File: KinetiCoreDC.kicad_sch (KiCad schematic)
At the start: 7 parts, among them J1 TC2070-IDC-NL, SW1 PTS647, U1 STM32G070KBT6

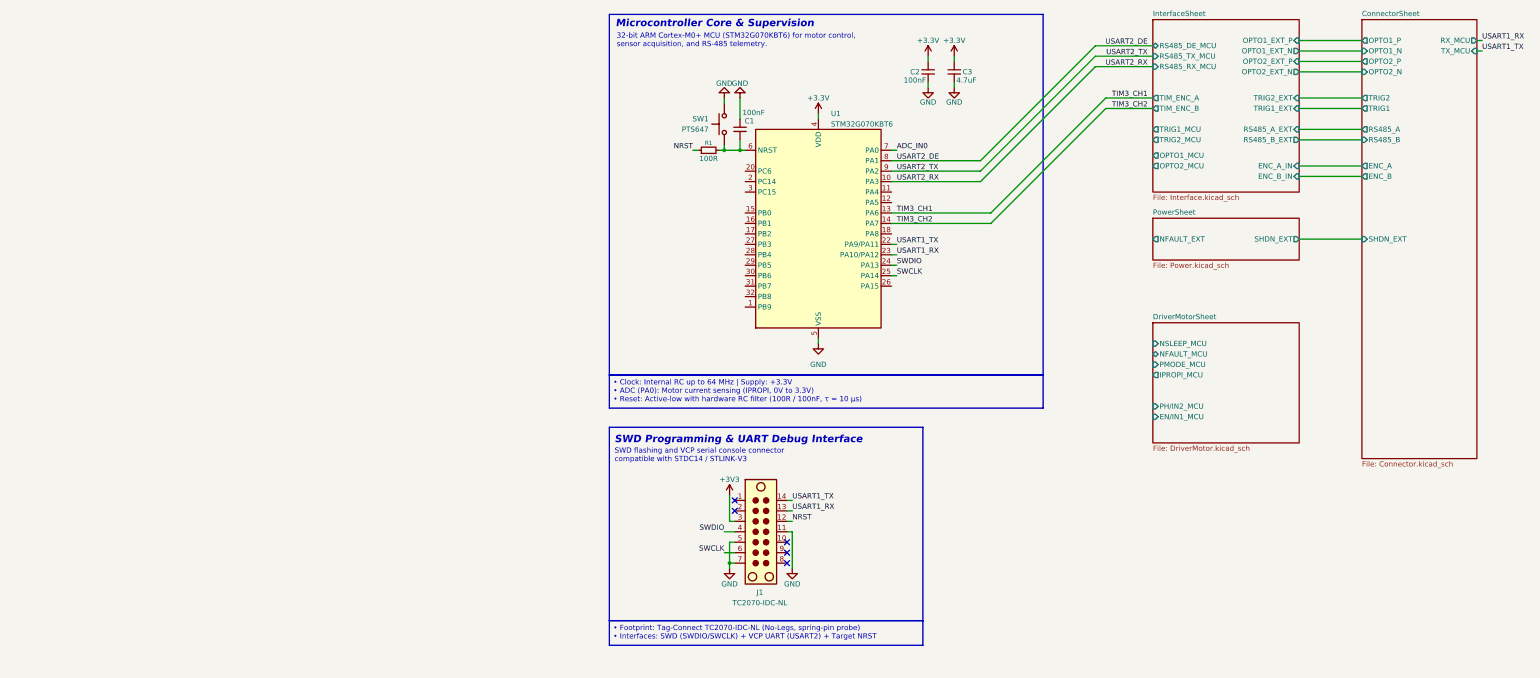
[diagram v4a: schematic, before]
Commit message: refactor(schematic): migrate MCU to LQFP48 and finalize pinout mapping
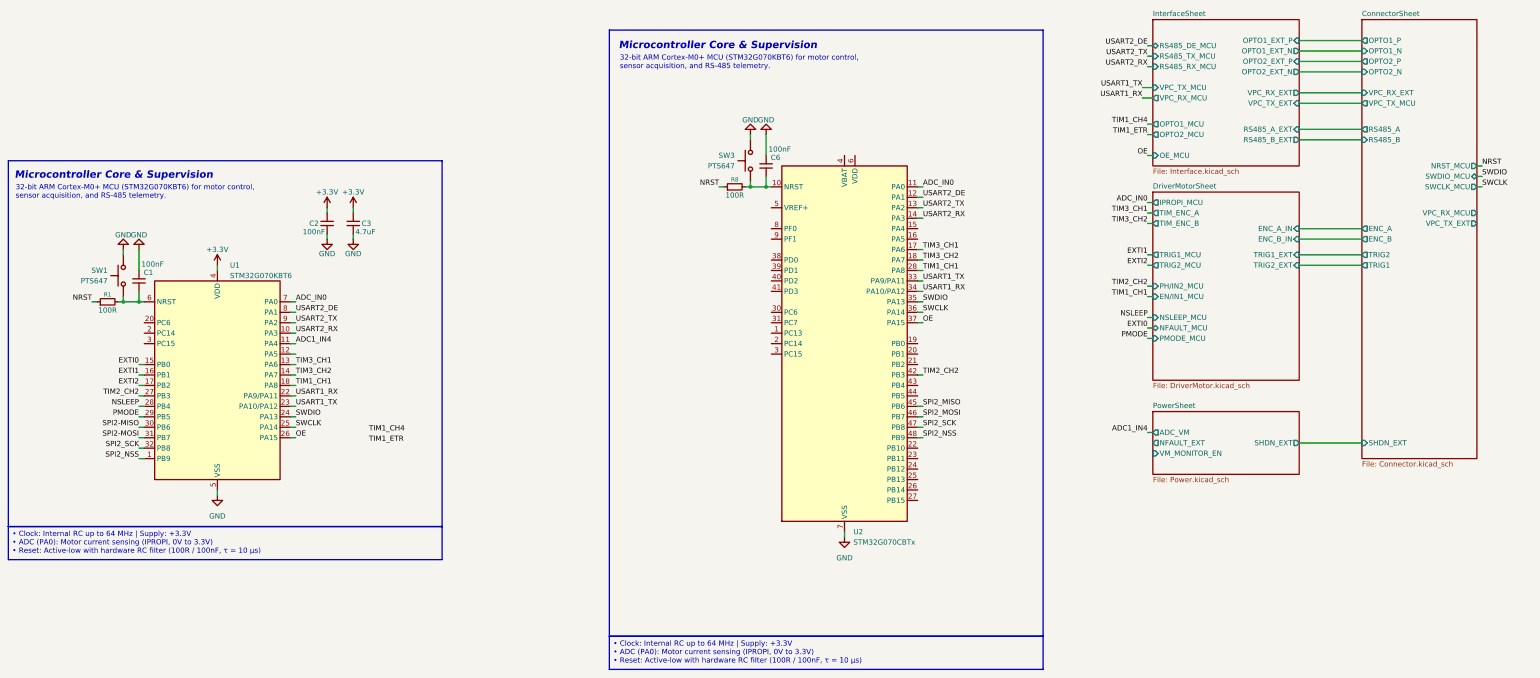
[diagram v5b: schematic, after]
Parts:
- removed J1: TC2070-IDC-NL, KineticCore:Tag-Connect_TC2070-IDC-FP_2x07_P1.27mm_Vertical, symbol Connector:TC2070
- added C6: 100nF, Capacitor_SMD:C_0603_1608Metric, symbol Device:C_Small
- added R8: 100R, Resistor_SMD:R_0603_1608Metric, symbol Device:R_Small
- added SW3: PTS647, Button_Switch_SMD:SW_SPST_PTS647_Sx38, symbol Switch:SW_Push
- added U2: STM32G070CBTx, Package_QFP:LQFP-48_7x7mm_P0.5mm, symbol MCU_ST_STM32G0:STM32G070CBTx
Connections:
- net ADC_IN0: now also U2.11 (PA0)
- net GND: now also C6.2, SW3.1, U2.7 (VSS)
- net NRST: now also R8.1
- net SWCLK: now also U2.36 (PA14)
- net SWDIO: now also U2.35 (PA13)
- net TIM3_CH1: now also U2.17 (PA6)
- net TIM3_CH2: now also U2.18 (PA7)
- net USART1_RX: now also U1.22 (PA9/PA11), U2.34 (PA10/PA12); no longer U1.23 (PA10/PA12)
- net USART1_TX: now also U1.23 (PA10/PA12), U2.33 (PA9/PA11); no longer U1.22 (PA9/PA11)
- net USART2_DE: now also U2.12 (PA1)
- net USART2_RX: now also U2.14 (PA3)
- net USART2_TX: now also U2.13 (PA2)
- net SPI2_NSS: now reaches U1.1 (PB9)
- net SPI2_NSS: now also U2.48 (PB9)
- net ADC1_IN4: now reaches U1.11 (PA4)
- net EXTI0: now reaches U1.15 (PB0)
- net EXTI1: now reaches U1.16 (PB1)
- net EXTI2: now reaches U1.17 (PB2)
- net TIM1_CH1: now reaches U1.18 (PA8)
- net TIM1_CH1: now also U2.28 (PA8)
- net OE: now reaches U1.26 (PA15)
- net OE: now also U2.37 (PA15)
- net TIM2_CH2: now reaches U1.27 (PB3)
- net TIM2_CH2: now also U2.42 (PB3)
- net NSLEEP: now reaches U1.28 (PB4)
- net PMODE: now reaches U1.29 (PB5)
- net SPI2-MISO: now reaches U1.30 (PB6)
- net SPI2-MOSI: now reaches U1.31 (PB7)
- net SPI2_SCK: now reaches U1.32 (PB8)
- net SPI2_SCK: now also U2.47 (PB8)
- new net: C6.1, R8.2, SW3.2, U2.10 (NRST)
- new net SPI2_MISO: U2.45 (PB6)
- new net SPI2_MOSI: U2.46 (PB7)
- no-connect marks 5 -> 0
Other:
- sheet ConnectorSheet ports: added NRST_MCU, SWCLK_MCU, SWDIO_MCU, VPC_RX_EXT, VPC_RX_MCU, VPC_TX_EXT, VPC_TX_MCU; removed RX_MCU, TX_MCU
- sheet DriverMotorSheet ports: added ENC_A_IN, ENC_B_IN, TIM_ENC_A, TIM_ENC_B, TRIG1_EXT, TRIG1_MCU, TRIG2_EXT, TRIG2_MCU; removed none
- sheet InterfaceSheet ports: added OE_MCU, VPC_RX_EXT, VPC_RX_MCU, VPC_TX_EXT, VPC_TX_MCU; removed ENC_A_IN, ENC_B_IN, TIM_ENC_A, TIM_ENC_B, TRIG1_EXT, TRIG1_MCU, TRIG2_EXT, TRIG2_MCU
- sheet PowerSheet ports: added ADC_VM, VM_MONITOR_EN; removed none
- note removed: "SWD Programming & UART Debug Interface"
- note removed: "SWD flashing and VCP serial console connector compatible with STDC14 / STLINK-V3"
- moved on the sheet: C1, C2, C3, R1, SW1, U1

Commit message: feat : add SMLVN6RGB status LED stage with balanced 3.3V ballast resistors
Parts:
- removed C1: 100nF, Capacitor_SMD:C_0603_1608Metric, symbol Device:C_Small
- removed R1: 100R, Resistor_SMD:R_0603_1608Metric, symbol Device:R_Small
- removed SW1: PTS647, Button_Switch_SMD:SW_SPST_PTS647_Sx38, symbol Switch:SW_Push
- removed U1: STM32G070KBT6, Package_QFP:LQFP-32_7x7mm_P0.8mm, symbol MCU_ST_STM32G0:STM32G070KBTx
- added C7: 100nF, Capacitor_SMD:C_0603_1608Metric, symbol Device:C_Small
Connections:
- net +3.3V is gone; now on net +3V3: C2.1, C3.1
- net GND: now also C7.2
- net +3V3: now reaches U2.4 (VBAT)
- net +3V3: now also U2.5 (VREF+), U2.6 (VDD), C7.1
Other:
- sheet DriverMotorSheet ports: added OUTA, OUTB; removed none
- sheet PowerSheet ports: added BLUE_MCU, GREEN_MCU, RED_MCU; removed none
- moved on the sheet: C2, C6, R8, SW3, U2

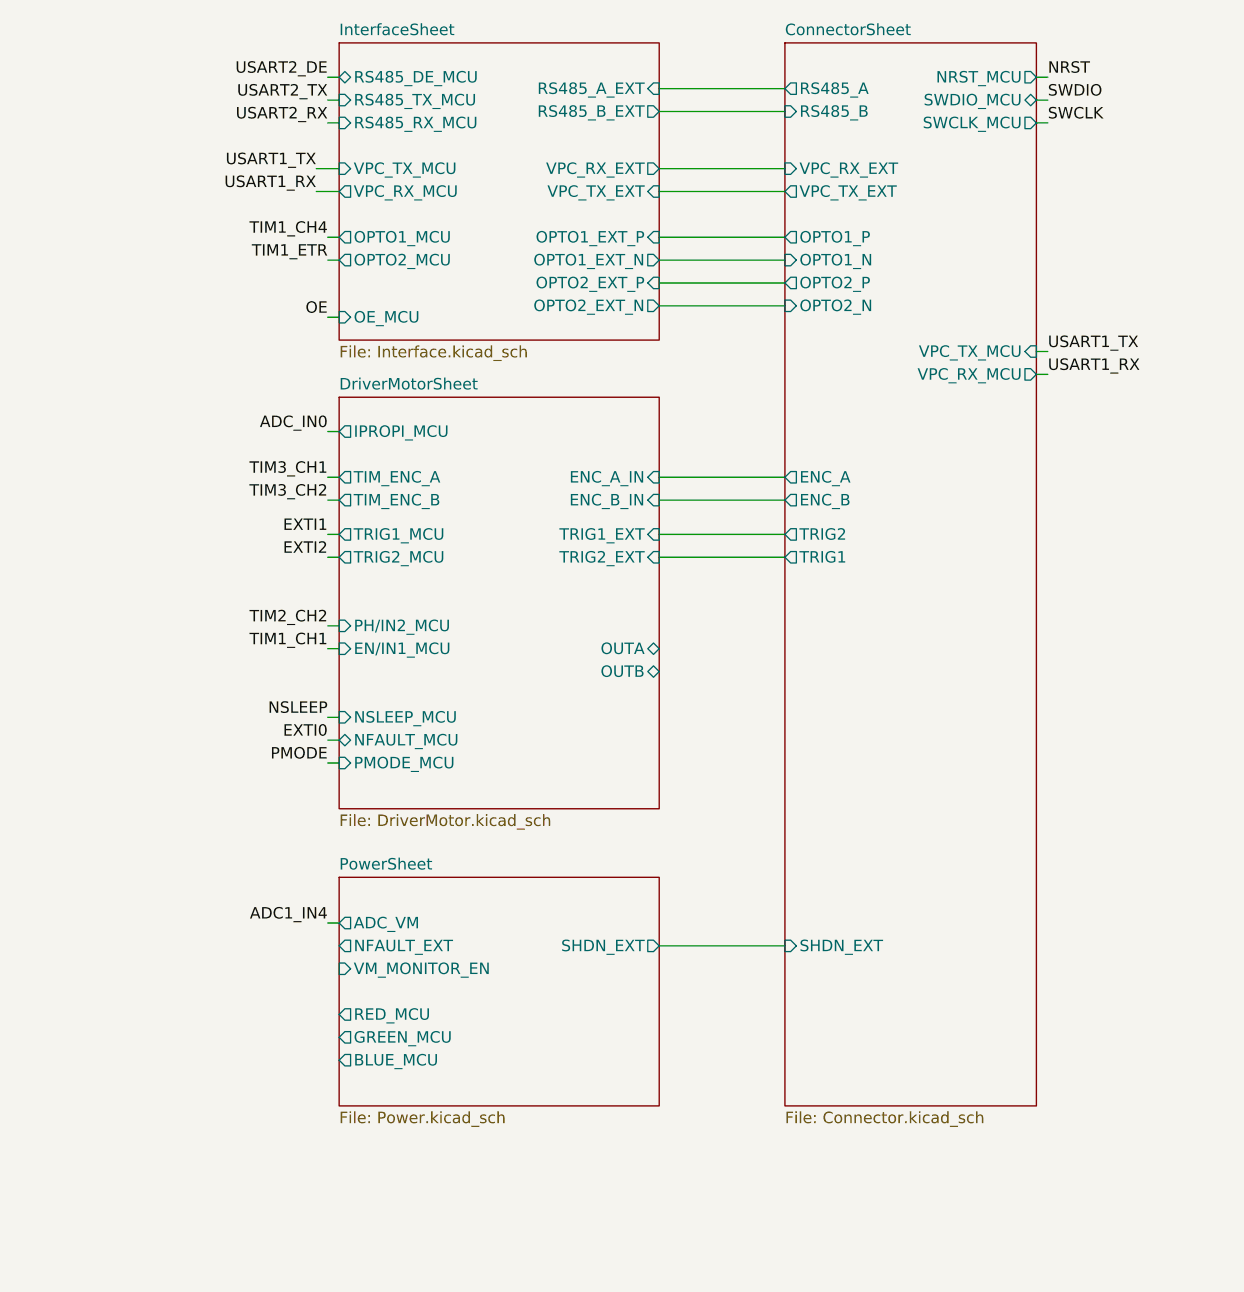
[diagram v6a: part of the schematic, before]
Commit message: feat: switch to JST-GH connectors and add TPD4E05U06 TVS protection for SPI/I2C
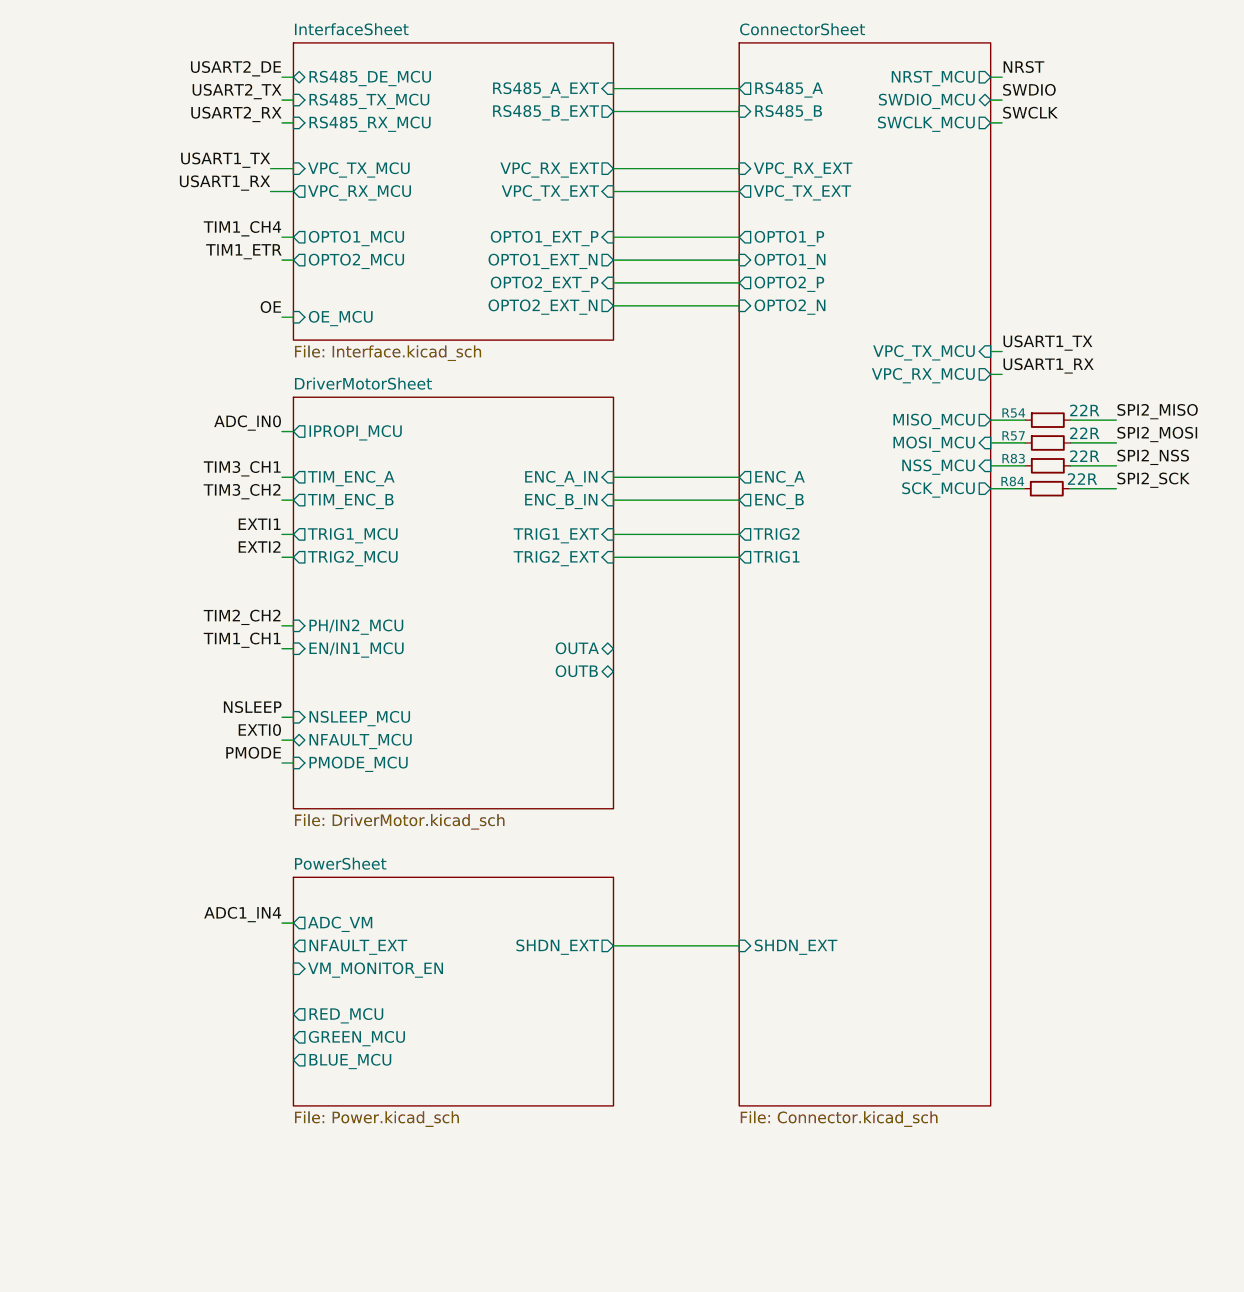
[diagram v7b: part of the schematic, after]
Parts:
- added R54, R57, R83, R84: 22R, Resistor_SMD:R_0603_1608Metric, symbol Device:R_Small
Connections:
- net SPI2_MISO: now also R54.2
- net SPI2_MOSI: now also R57.2
- net SPI2_NSS: now also R83.2
- net SPI2_SCK: now also R84.2
- new net ConnectorSheet/MISO_MCU: R54.1
- new net ConnectorSheet/MOSI_MCU: R57.1
- new net ConnectorSheet/NSS_MCU: R83.1
- new net ConnectorSheet/SCK_MCU: R84.1
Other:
- sheet ConnectorSheet ports: added MISO_MCU, MOSI_MCU, NSS_MCU, SCK_MCU; removed none

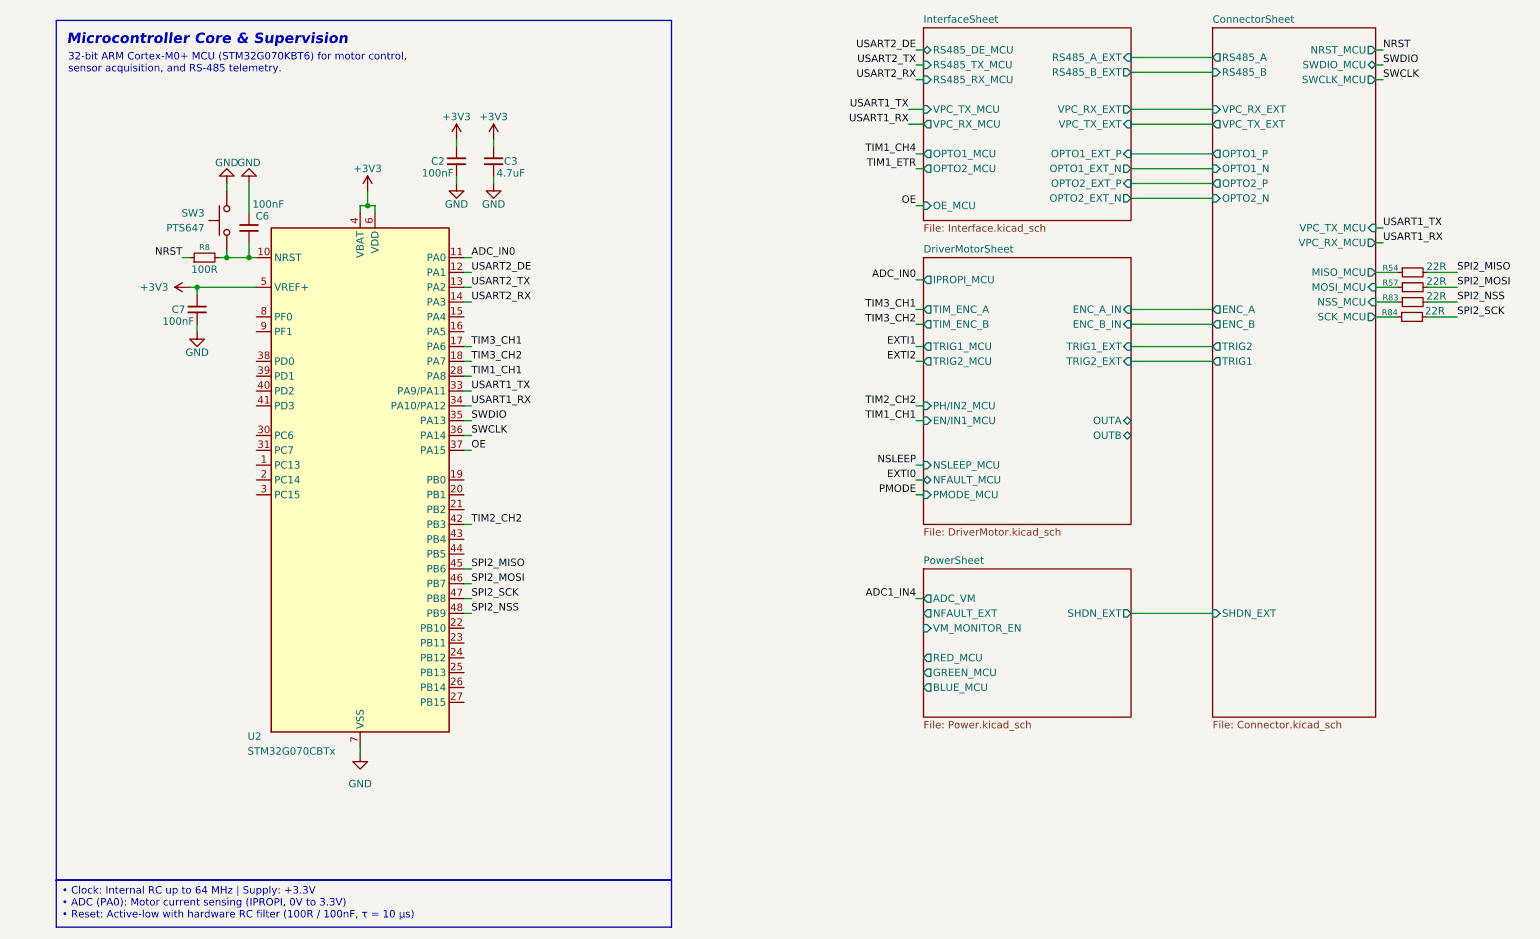
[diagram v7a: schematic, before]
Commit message: feat: finalize STM32G070CBT6 LQFP48 pinout and peripheral mapping
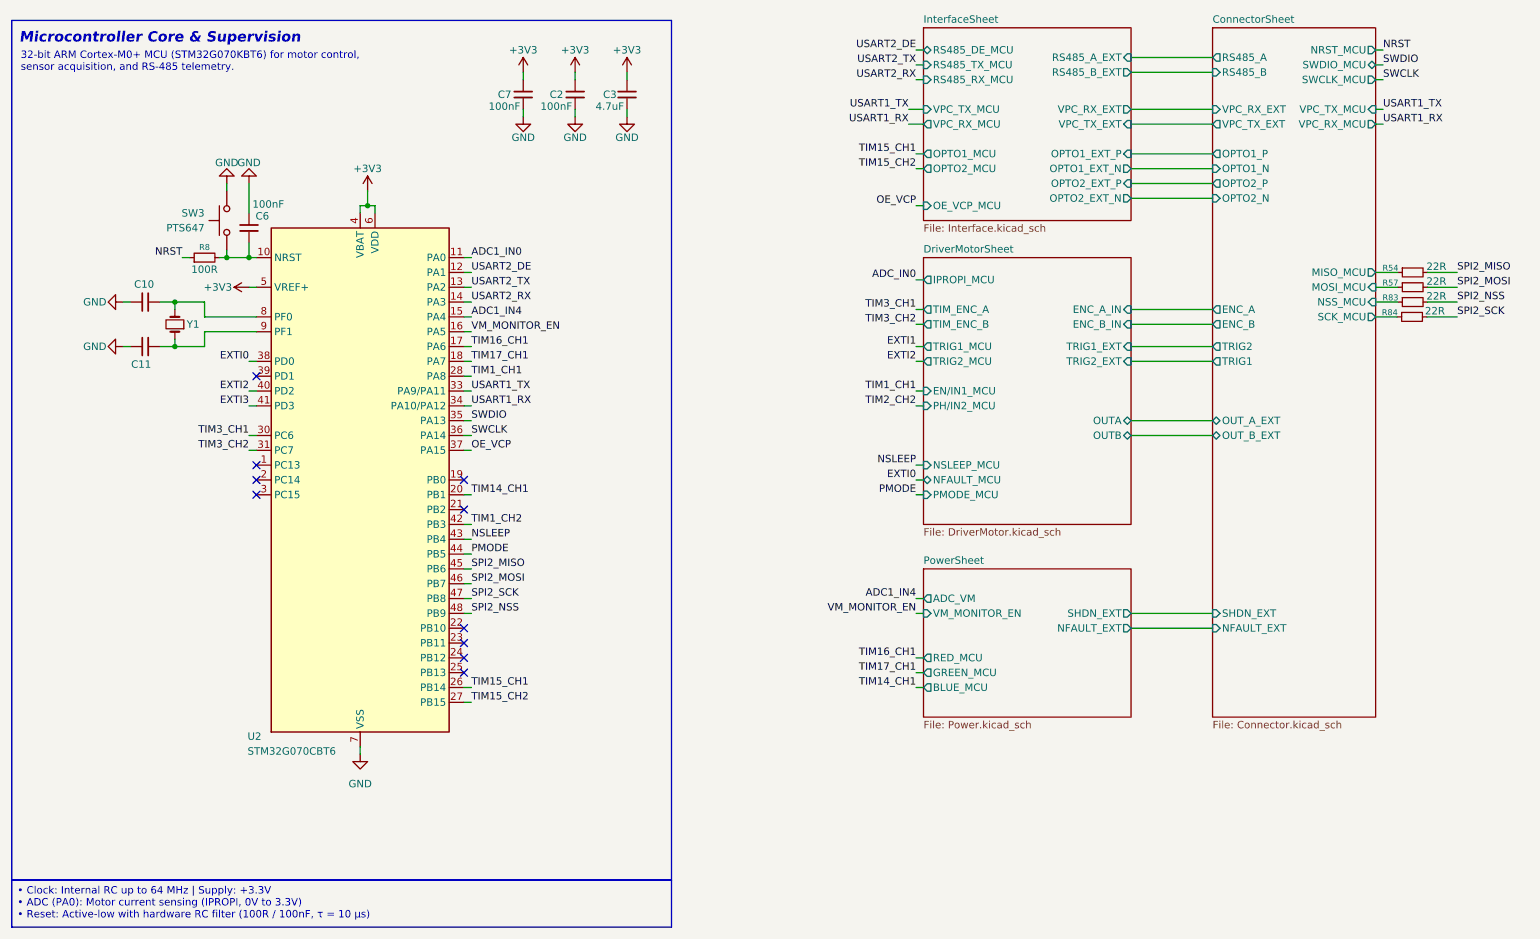
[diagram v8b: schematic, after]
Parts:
- added C10, C11: 100nF, Capacitor_SMD:C_0603_1608Metric, symbol Device:C_Small
- added Y1: Crystal_Small, Oscillator:Oscillator_SMD_IDT_JS6-6_5.0x3.2mm_P1.27mm, symbol Device:Crystal_Small
- U2: value STM32G070CBTx -> STM32G070CBT6
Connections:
- net ADC1_IN4: now also U2.15 (PA4)
- net ADC_IN0: no longer U2.11 (PA0)
- net EXTI0: now also U2.38 (PD0)
- net EXTI2: now also U2.40 (PD2)
- net GND: now also C10.2, C11.2
- net NSLEEP: now also U2.43 (PB4)
- net PMODE: now also U2.44 (PB5)
- net TIM2_CH2: no longer U2.42 (PB3)
- net TIM3_CH1: now also U2.30 (PC6); no longer U2.17 (PA6)
- net TIM3_CH2: now also U2.31 (PC7); no longer U2.18 (PA7)
- net VM_MONITOR_EN: now reaches U2.16 (PA5)
- net TIM14_CH1: now reaches U2.20 (PB1)
- net TIM15_CH1: now reaches U2.26 (PB14)
- net TIM15_CH2: now reaches U2.27 (PB15)
- net EXTI3: now reaches U2.41 (PD3)
- net at U2.8 (PF0): now also C10.1, Y1.2
- net at U2.9 (PF1): now also C11.1, Y1.1
- net OE renamed OE_VCP
- new net ADC1_IN0: U2.11 (PA0)
- new net TIM16_CH1: U2.17 (PA6)
- new net TIM17_CH1: U2.18 (PA7)
- new net TIM1_CH2: U2.42 (PB3)
- no-connect marks 0 -> 10
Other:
- sheet ConnectorSheet ports: added NFAULT_EXT, OUT_A_EXT, OUT_B_EXT; removed none
- sheet InterfaceSheet ports: added OE_VCP_MCU; removed OE_MCU
- moved on the sheet: C2, C3
